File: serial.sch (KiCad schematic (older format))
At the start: 9 parts, among them CN13 RS232, IC1 MAX3232CPWR, J1 TTL, T6 TEST_RS232

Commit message: finished schematic and PCB layout for 1.1 board
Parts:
- removed J1: TTL, telemetry-pcb:molex_sl_1x04_horizontal, symbol Connector:Conn_01x04_Male
- added CN4: UART, telemetry-pcb:Molex-70551-0004-0, symbol Connector_Generic:Conn_01x05
- added J1: Header 02x02, Connector_PinHeader_2.54mm:PinHeader_2x02_P2.54mm_Horizontal, symbol Connector_Generic:Conn_02x02_Odd_Even
- added J2: Header 02x03, Connector_PinHeader_2.54mm:PinHeader_2x03_P2.54mm_Horizontal, symbol Connector_Generic:Conn_02x03_Odd_Even
- added Q1: IF-D92, telemetry-pcb:IF-D92, symbol Device:Q_Photo_NPN
- added R7: 10K, Resistor_SMD:R_0805_2012Metric, symbol Device:R
- renumbered CN13 to CN3, T6 to T5
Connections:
- wire segments 41 -> 64
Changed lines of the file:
@@
 $Descr A4 11693 8268
 encoding utf-8
-Sheet 3 4
+Sheet 2 3
 Title ""
 Date ""
@@
 P 6150 4600
 AR Path="/6199B42E" Ref="#PWR?"  Part="1"
-AR Path="/61951597/6199B42E" Ref="#PWR0119"  Part="1"
-F 0 "#PWR0119" H 6150 4350 50  0001 C CNN
+AR Path="/61951597/6199B42E" Ref="#PWR013"  Part="1"
+F 0 "#PWR013" H 6150 4350 50  0001 C CNN
 F 1 "GND" H 6155 4427 50  0000 C CNN
 F 2 "" H 6150 4600 50  0001 C CNN
@@
 P 6350 2500
 AR Path="/6199B436" Ref="#PWR?"  Part="1"
-AR Path="/61951597/6199B436" Ref="#PWR0120"  Part="1"
-F 0 "#PWR0120" H 6350 2350 50  0001 C CNN
+AR Path="/61951597/6199B436" Ref="#PWR014"  Part="1"
+F 0 "#PWR014" H 6350 2350 50  0001 C CNN
 F 1 "+3V3" H 6365 2673 50  0000 C CNN
 F 2 "" H 6350 2500 50  0001 C CNN
@@
 Wire Wire Line
 	4600 3400 4350 3400
-Text HLabel 9600 3600 2    100  Output ~ 0
+Text HLabel 10450 3000 2    100  Output ~ 0
 RX
-$Comp
-L Connector:Conn_01x04_Male J1
-U 1 1 61C3A8C7
-P 8300 2700
-F 0 "J1" H 8408 2981 50  0000 C CNN
-F 1 "TTL" H 8408 2890 50  0000 C CNN
-F 2 "telemetry-pcb:molex_sl_1x04_horizontal" H 8300 2700 50  0001 C CNN
-F 3 "~" H 8300 2700 50  0001 C CNN
-	1    8300 2700
-	1    0    0    -1
-$EndComp
-Wire Wire Line
-	9600 1900 8700 1900
-Text HLabel 9600 1900 2    100  Output ~ 0
+Text HLabel 10450 2400 2    100  Output ~ 0
 TX
 Wire Wire Line
-	8700 2600 8500 2600
-Connection ~ 8700 1900
-Wire Wire Line
-	8500 2700 8700 2700
-Wire Wire Line
-	8500 2800 8700 2800
-Wire Wire Line
-	8700 3600 9600 3600
-Wire Wire Line
-	8500 2900 8700 2900
-Wire Wire Line
 	4350 1900 4350 3400
-Connection ~ 8700 3600
-Wire Wire Line
-	8700 1900 8700 2600
-Connection ~ 8700 2600
-Wire Wire Line
-	8700 2600 8700 2700
-Wire Wire Line
-	8700 2800 8700 2900
-Connection ~ 8700 2900
-Wire Wire Line
-	8700 2900 8700 3600
 NoConn ~ 7150 5200
 NoConn ~ 7150 5100
@@
 NoConn ~ 7150 4600
 NoConn ~ 7150 4500
-NoConn ~ 7150 4400
 $Comp
 L Connector:Conn_01x02_Female T?
@@
 P 6850 5450
 AR Path="/6199B41D" Ref="T?"  Part="1"
-AR Path="/61951597/6199B41D" Ref="T6"  Part="1"
-F 0 "T6" V 6696 5262 50  0000 R CNN
+AR Path="/61951597/6199B41D" Ref="T5"  Part="1"
+F 0 "T5" V 6696 5262 50  0000 R CNN
 F 1 "TEST_RS232" V 6787 5262 50  0000 R CNN
 F 2 "TestPoint:TestPoint_2Pads_Pitch2.54mm_Drill0.8mm" H 6850 5450 50  0001 C CNN
@@
 P 7450 4800
 AR Path="/6199B3ED" Ref="CN?"  Part="1"
-AR Path="/61951597/6199B3ED" Ref="CN13"  Part="1"
-F 0 "CN13" H 7630 4846 50  0000 L CNN
+AR Path="/61951597/6199B3ED" Ref="CN3"  Part="1"
+F 0 "CN3" H 7630 4846 50  0000 L CNN
 F 1 "RS232" H 7630 4755 50  0000 L CNN
 F 2 "telemetry-pcb:db-9" H 7450 4800 50  0001 C CNN
@@
 P 7050 3300
 AR Path="/6199B40A" Ref="#SUPPLY?"  Part="1"
-AR Path="/61951597/6199B40A" Ref="#SUPPLY0101"  Part="1"
-F 0 "#SUPPLY0101" H 7050 3300 50  0001 C CNN
+AR Path="/61951597/6199B40A" Ref="#SUPPLY01"  Part="1"
+F 0 "#SUPPLY01" H 7050 3300 50  0001 C CNN
 F 1 "GND" H 7050 3200 59  0000 C CNN
 F 2 "" H 7050 3300 50  0001 C CNN
@@
 	6850 5000 7150 5000
 Wire Wire Line
-	4350 1900 8700 1900
-Wire Wire Line
-	6000 3600 8700 3600
+	7150 4400 7000 4400
+Wire Wire Line
+	7000 4400 7000 4100
+Wire Wire Line
+	7000 4100 8250 4100
+$Comp
+L telemetry-pcb-rescue:GND-telemetry-pcb-eagle-import-telemetry-pcb-rescue #SUPPLY?
+U 1 1 62526122
+P 8250 4700
+AR Path="/62526122" Ref="#SUPPLY?"  Part="1"
+AR Path="/61951597/62526122" Ref="#SUPPLY02"  Part="1"
+F 0 "#SUPPLY02" H 8250 4700 50  0001 C CNN
+F 1 "GND" H 8250 4600 59  0000 C CNN
+F 2 "" H 8250 4700 50  0001 C CNN
+F 3 "" H 8250 4700 50  0001 C CNN
+	1    8250 4700
+	1    0    0    -1
+$EndComp
+Wire Wire Line
+	4350 1900 8950 1900
+$Comp
+L Device:Q_Photo_NPN Q1
+U 1 1 625465A1
+P 9250 3650
+F 0 "Q1" H 9440 3696 50  0000 L CNN
+F 1 "IF-D92" H 9440 3605 50  0000 L CNN
+F 2 "telemetry-pcb:IF-D92" H 9450 3750 50  0001 C CNN
+F 3 "~" H 9250 3650 50  0001 C CNN
+	1    9250 3650
+	1    0    0    -1
+$EndComp
+$Comp
+L Device:R R7
+U 1 1 625499FE
+P 9350 4150
+F 0 "R7" H 9420 4196 50  0000 L CNN
+F 1 "10K" H 9420 4105 50  0000 L CNN
+F 2 "Resistor_SMD:R_0805_2012Metric" V 9280 4150 50  0001 C CNN
+F 3 "~" H 9350 4150 50  0001 C CNN
+	1    9350 4150
+	1    0    0    -1
+$EndComp
+Wire Wire Line
+	10050 2350 10250 2350
+Wire Wire Line
+	10250 2350 10250 2400
+Wire Wire Line
+	10250 2400 10450 2400
+Wire Wire Line
+	10050 2450 10250 2450
+Wire Wire Line
+	10250 2450 10250 2400
+Connection ~ 10250 2400
+$Comp
+L Connector_Generic:Conn_02x02_Odd_Even J1
+U 1 1 6254B4AA
+P 9750 2350
+F 0 "J1" H 9800 2567 50  0000 C CNN
+F 1 "Header 02x02" H 9800 2476 50  0000 C CNN
+F 2 "Connector_PinHeader_2.54mm:PinHeader_2x02_P2.54mm_Horizontal" H 9750 2350 50  0001 C CNN
+F 3 "~" H 9750 2350 50  0001 C CNN
+	1    9750 2350
+	1    0    0    -1
+$EndComp
+Wire Wire Line
+	8950 1900 8950 2350
+$Comp
+L Connector_Generic:Conn_01x05 CN4
+U 1 1 62553AD4
+P 7800 2550
+F 0 "CN4" H 7718 2125 50  0000 C CNN
+F 1 "UART" H 7718 2216 50  0000 C CNN
+F 2 "telemetry-pcb:Molex-70551-0004-0" H 7800 2550 50  0001 C CNN
+F 3 "~" H 7800 2550 50  0001 C CNN
+	1    7800 2550
+	-1   0    0    1
+$EndComp
+Wire Wire Line
+	8000 2450 9550 2450
+$Comp
+L power:+3V3 #PWR?
+U 1 1 6255A3E2
+P 8250 2250
+AR Path="/6255A3E2" Ref="#PWR?"  Part="1"
+AR Path="/61951597/6255A3E2" Ref="#PWR015"  Part="1"
+F 0 "#PWR015" H 8250 2100 50  0001 C CNN
+F 1 "+3V3" H 8265 2423 50  0000 C CNN
+F 2 "" H 8250 2250 50  0001 C CNN
+F 3 "" H 8250 2250 50  0001 C CNN
+	1    8250 2250
+	1    0    0    -1
+$EndComp
+Wire Wire Line
+	8000 2350 8250 2350
+Wire Wire Line
+	8250 2350 8250 2250
+$Comp
+L Connector_Generic:Conn_02x03_Odd_Even J2
+U 1 1 6255DD8F
+P 9750 3000
+F 0 "J2" H 9800 3317 50  0000 C CNN
+F 1 "Header 02x03" H 9800 3226 50  0000 C CNN
+F 2 "Connector_PinHeader_2.54mm:PinHeader_2x03_P2.54mm_Horizontal" H 9750 3000 50  0001 C CNN
+F 3 "~" H 9750 3000 50  0001 C CNN
+	1    9750 3000
+	1    0    0    -1
+$EndComp
+Wire Wire Line
+	6000 3600 8950 3600
+Wire Wire Line
+	10050 2900 10250 2900
+Wire Wire Line
+	10250 2900 10250 3000
+Wire Wire Line
+	10250 3000 10450 3000
+Wire Wire Line
+	10050 3000 10250 3000
+Connection ~ 10250 3000
+Wire Wire Line
+	10050 3100 10250 3100
+Wire Wire Line
+	10250 3100 10250 3000
+Wire Wire Line
+	8000 2650 8700 2650
+Wire Wire Line
+	8950 2900 9550 2900
+Wire Wire Line
+	8950 2350 9550 2350
+Wire Wire Line
+	8950 2900 8950 3600
+Wire Wire Line
+	8700 3000 9550 3000
+Wire Wire Line
+	8700 2650 8700 3000
+Wire Wire Line
+	9350 3100 9550 3100
+Wire Wire Line
+	9350 3100 9350 3450
+Wire Wire Line
+	9350 3850 9350 4000
+Wire Wire Line
+	8250 4100 8250 4450
+Wire Wire Line
+	9350 4300 9350 4450
+Wire Wire Line
+	9350 4450 8250 4450
+Connection ~ 8250 4450
+Wire Wire Line
+	8250 4450 8250 4600
+Wire Wire Line
+	8000 2750 8000 3200
+Wire Wire Line
+	8000 3200 7050 3200
+NoConn ~ 8000 2550
 $EndSCHEMATC

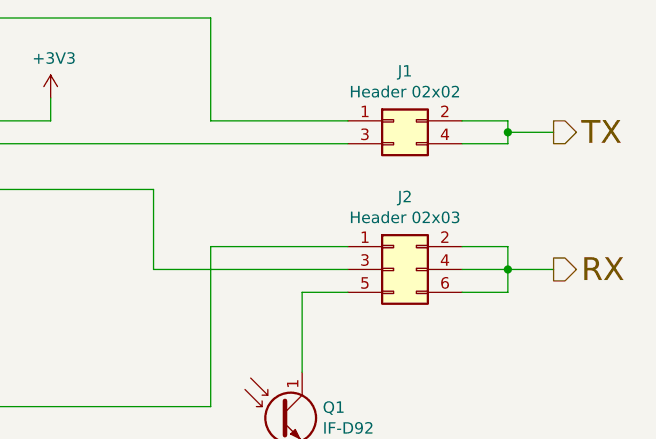
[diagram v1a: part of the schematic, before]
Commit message: removes one power port, changes CAN switch to jumper
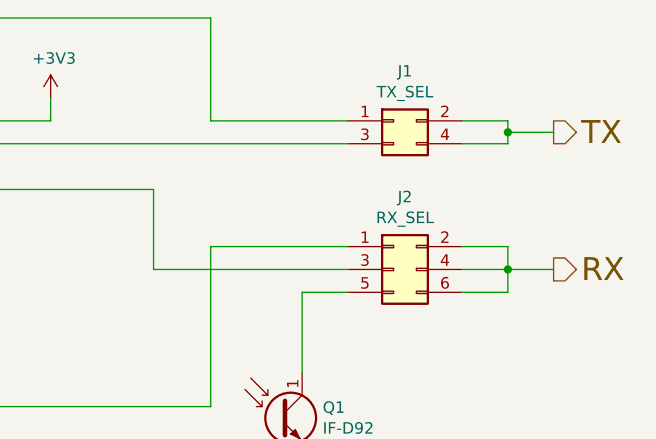
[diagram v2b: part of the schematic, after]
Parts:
- J1: value Header 02x02 -> TX_SEL
- J2: value Header 02x03 -> RX_SEL
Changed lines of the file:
@@
 P 9750 2350
 F 0 "J1" H 9800 2567 50  0000 C CNN
-F 1 "Header 02x02" H 9800 2476 50  0000 C CNN
+F 1 "TX_SEL" H 9800 2476 50  0000 C CNN
 F 2 "Connector_PinHeader_2.54mm:PinHeader_2x02_P2.54mm_Horizontal" H 9750 2350 50  0001 C CNN
 F 3 "~" H 9750 2350 50  0001 C CNN
@@
 P 9750 3000
 F 0 "J2" H 9800 3317 50  0000 C CNN
-F 1 "Header 02x03" H 9800 3226 50  0000 C CNN
+F 1 "RX_SEL" H 9800 3226 50  0000 C CNN
 F 2 "Connector_PinHeader_2.54mm:PinHeader_2x03_P2.54mm_Horizontal" H 9750 3000 50  0001 C CNN
 F 3 "~" H 9750 3000 50  0001 C CNN

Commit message: deleted extraneous footprints
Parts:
- IC1: symbol telemetry-pcb-rescue:MAX3232CPWR-MAX3232CPWR-telemetry-pcb-rescue -> telemetry-pcb-rescue:MAX3232CPWR-MAX3232CPWR-telemetry-pcb-rescue-telemetry-pcb-rescue
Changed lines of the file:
@@
 $EndComp
 $Comp
-L telemetry-pcb-rescue:MAX3232CPWR-MAX3232CPWR-telemetry-pcb-rescue IC?
+L telemetry-pcb-rescue:MAX3232CPWR-MAX3232CPWR-telemetry-pcb-rescue-telemetry-pcb-rescue IC?
 U 1 1 6199B43C
 P 5300 3800
@@
 	7050 2800 7050 3200
 $Comp
-L telemetry-pcb-rescue:GND-telemetry-pcb-eagle-import-telemetry-pcb-rescue #SUPPLY?
+L telemetry-pcb-rescue:GND-telemetry-pcb-eagle-import-telemetry-pcb-rescue-telemetry-pcb-rescue #SUPPLY?
 U 1 1 6199B40A
 P 7050 3300
@@
 	7000 4100 8250 4100
 $Comp
-L telemetry-pcb-rescue:GND-telemetry-pcb-eagle-import-telemetry-pcb-rescue #SUPPLY?
+L telemetry-pcb-rescue:GND-telemetry-pcb-eagle-import-telemetry-pcb-rescue-telemetry-pcb-rescue #SUPPLY?
 U 1 1 62526122
 P 8250 4700

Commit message: minor changes to serial port - update rs232 connector and delete GND connection
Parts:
- CN3: footprint telemetry-pcb:db-9 -> Connector_Dsub:DSUB-9_Female_Horizontal_P2.77x2.84mm_EdgePinOffset7.70mm_Housed_MountingHolesOffset9.12mm; symbol Connector:DB9_Male -> Connector:DB9_Female
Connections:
- net at IC1.14 (DOUT1), T5.1 (Pin_1): now also CN3.3; no longer CN3.2
- net at IC1.13 (RIN1), T5.2 (Pin_2): now also CN3.2; no longer CN3.3
- net at CN3.5: no longer R7.2
- no-connect marks 11 -> 12
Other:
- moved on the sheet: T5
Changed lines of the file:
@@
 $EndComp
-Wire Wire Line
-	4050 3600 4050 4800
 Wire Wire Line
 	4600 3400 4350 3400
@@
 Wire Wire Line
 	4350 1900 4350 3400
-NoConn ~ 7150 5200
 NoConn ~ 7150 5100
 NoConn ~ 7150 4900
 NoConn ~ 7150 4700
-NoConn ~ 7150 4600
 NoConn ~ 7150 4500
 $Comp
 L Connector:Conn_01x02_Female T?
 U 1 1 6199B41D
-P 6850 5450
+P 6750 5350
 AR Path="/6199B41D" Ref="T?"  Part="1"
 AR Path="/61951597/6199B41D" Ref="T5"  Part="1"
-F 0 "T5" V 6696 5262 50  0000 R CNN
-F 1 "TEST_RS232" V 6787 5262 50  0000 R CNN
-F 2 "TestPoint:TestPoint_2Pads_Pitch2.54mm_Drill0.8mm" H 6850 5450 50  0001 C CNN
-F 3 "~" H 6850 5450 50  0001 C CNN
-	1    6850 5450
+F 0 "T5" V 6596 5162 50  0000 R CNN
+F 1 "TEST_RS232" V 6687 5162 50  0000 R CNN
+F 2 "TestPoint:TestPoint_2Pads_Pitch2.54mm_Drill0.8mm" H 6750 5350 50  0001 C CNN
+F 3 "~" H 6750 5350 50  0001 C CNN
+	1    6750 5350
 	0    1    1    0
 $EndComp
 $Comp
-L Connector:DB9_Male CN?
+L Connector:DB9_Female CN?
 U 1 1 6199B3ED
 P 7450 4800
@@
 F 0 "CN3" H 7630 4846 50  0000 L CNN
 F 1 "RS232" H 7630 4755 50  0000 L CNN
-F 2 "telemetry-pcb:db-9" H 7450 4800 50  0001 C CNN
+F 2 "Connector_Dsub:DSUB-9_Female_Horizontal_P2.77x2.84mm_EdgePinOffset7.70mm_Housed_MountingHolesOffset9.12mm" H 7450 4800 50  0001 C CNN
 F 3 " ~" H 7450 4800 50  0001 C CNN
 	1    7450 4800
@@
 	6350 2800 6350 3100
 Wire Wire Line
-	6850 5250 6850 5000
-Connection ~ 6850 5000
-Wire Wire Line
-	4050 4800 6750 4800
-Wire Wire Line
-	6850 3400 6850 5000
+	4050 5000 6650 5000
 Wire Wire Line
 	6000 3400 6850 3400
-Wire Wire Line
-	6750 4800 6750 5250
-Connection ~ 6750 4800
-Wire Wire Line
-	6750 4800 7150 4800
-Wire Wire Line
-	6850 5000 7150 5000
-Wire Wire Line
-	7150 4400 7000 4400
-Wire Wire Line
-	7000 4400 7000 4100
-Wire Wire Line
-	7000 4100 8250 4100
 $Comp
 L telemetry-pcb-rescue:GND-telemetry-pcb-eagle-import-telemetry-pcb-rescue-telemetry-pcb-rescue #SUPPLY?
 U 1 1 62526122
-P 8250 4700
+P 9350 4550
 AR Path="/62526122" Ref="#SUPPLY?"  Part="1"
 AR Path="/61951597/62526122" Ref="#SUPPLY02"  Part="1"
-F 0 "#SUPPLY02" H 8250 4700 50  0001 C CNN
-F 1 "GND" H 8250 4600 59  0000 C CNN
-F 2 "" H 8250 4700 50  0001 C CNN
-F 3 "" H 8250 4700 50  0001 C CNN
-	1    8250 4700
+F 0 "#SUPPLY02" H 9350 4550 50  0001 C CNN
+F 1 "GND" H 9350 4450 59  0000 C CNN
+F 2 "" H 9350 4550 50  0001 C CNN
+F 3 "" H 9350 4550 50  0001 C CNN
+	1    9350 4550
 	1    0    0    -1
 $EndComp
@@
 	9350 3850 9350 4000
 Wire Wire Line
-	8250 4100 8250 4450
-Wire Wire Line
 	9350 4300 9350 4450
-Wire Wire Line
-	9350 4450 8250 4450
-Connection ~ 8250 4450
-Wire Wire Line
-	8250 4450 8250 4600
 Wire Wire Line
 	8000 2750 8000 3200
@@
 	8000 3200 7050 3200
 NoConn ~ 8000 2550
+NoConn ~ 7150 4400
+Wire Wire Line
+	6850 3400 6850 4800
+Wire Wire Line
+	6850 4800 7150 4800
+Wire Wire Line
+	4050 3600 4050 5000
+Wire Wire Line
+	6650 4600 6650 5000
+Wire Wire Line
+	6650 4600 7150 4600
+NoConn ~ 7150 5000
+Wire Wire Line
+	6650 5000 6650 5150
+Connection ~ 6650 5000
+Wire Wire Line
+	6850 4800 6850 5150
+Wire Wire Line
+	6850 5150 6750 5150
+Connection ~ 6850 4800
+NoConn ~ 7150 5200
 $EndSCHEMATC

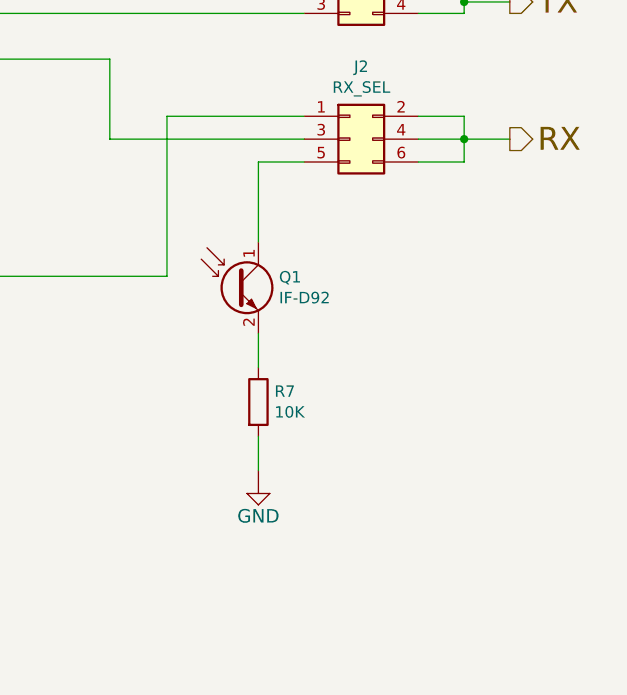
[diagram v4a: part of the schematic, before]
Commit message: fixes optical receiver wiring and changes GPS connector to JST GH
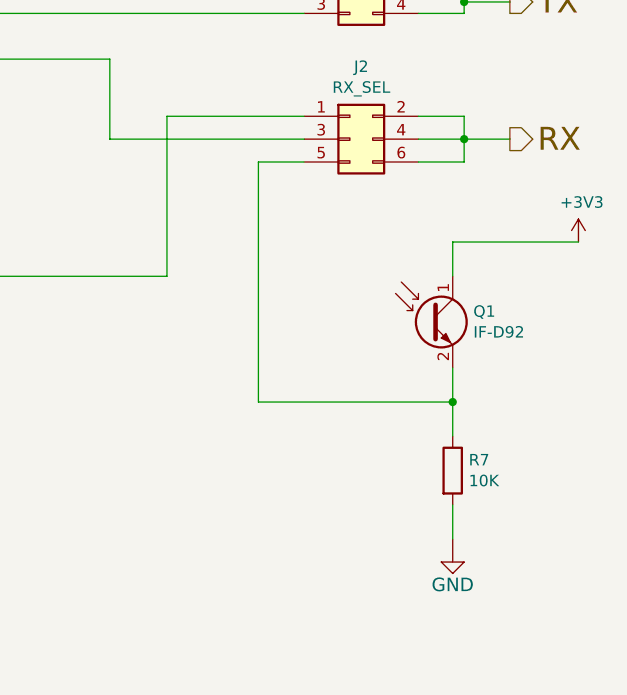
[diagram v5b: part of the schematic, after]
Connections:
- net +3V3: now also Q1.1 (C)
- net at J2.5 (Pin_5): now also Q1.2 (E), R7.1; no longer Q1.1 (C)
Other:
- moved on the sheet: Q1, R7
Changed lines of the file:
@@
 L telemetry-pcb-rescue:GND-telemetry-pcb-eagle-import-telemetry-pcb-rescue-telemetry-pcb-rescue #SUPPLY?
 U 1 1 62526122
-P 9350 4550
+P 10200 4850
 AR Path="/62526122" Ref="#SUPPLY?"  Part="1"
 AR Path="/61951597/62526122" Ref="#SUPPLY02"  Part="1"
-F 0 "#SUPPLY02" H 9350 4550 50  0001 C CNN
-F 1 "GND" H 9350 4450 59  0000 C CNN
-F 2 "" H 9350 4550 50  0001 C CNN
-F 3 "" H 9350 4550 50  0001 C CNN
-	1    9350 4550
+F 0 "#SUPPLY02" H 10200 4850 50  0001 C CNN
+F 1 "GND" H 10200 4750 59  0000 C CNN
+F 2 "" H 10200 4850 50  0001 C CNN
+F 3 "" H 10200 4850 50  0001 C CNN
+	1    10200 4850
 	1    0    0    -1
 $EndComp
@@
 L Device:Q_Photo_NPN Q1
 U 1 1 625465A1
-P 9250 3650
-F 0 "Q1" H 9440 3696 50  0000 L CNN
-F 1 "IF-D92" H 9440 3605 50  0000 L CNN
-F 2 "telemetry-pcb:IF-D92" H 9450 3750 50  0001 C CNN
-F 3 "~" H 9250 3650 50  0001 C CNN
-	1    9250 3650
+P 10100 3800
+F 0 "Q1" H 10290 3846 50  0000 L CNN
+F 1 "IF-D92" H 10290 3755 50  0000 L CNN
+F 2 "telemetry-pcb:IF-D92" H 10300 3900 50  0001 C CNN
+F 3 "~" H 10100 3800 50  0001 C CNN
+	1    10100 3800
 	1    0    0    -1
 $EndComp
@@
 L Device:R R7
 U 1 1 625499FE
-P 9350 4150
-F 0 "R7" H 9420 4196 50  0000 L CNN
-F 1 "10K" H 9420 4105 50  0000 L CNN
-F 2 "Resistor_SMD:R_0805_2012Metric" V 9280 4150 50  0001 C CNN
-F 3 "~" H 9350 4150 50  0001 C CNN
-	1    9350 4150
+P 10200 4450
+F 0 "R7" H 10270 4496 50  0000 L CNN
+F 1 "10K" H 10270 4405 50  0000 L CNN
+F 2 "Resistor_SMD:R_0805_2012Metric" V 10130 4450 50  0001 C CNN
+F 3 "~" H 10200 4450 50  0001 C CNN
+	1    10200 4450
 	1    0    0    -1
 $EndComp
@@
 	9350 3100 9550 3100
 Wire Wire Line
-	9350 3100 9350 3450
+	10200 4150 10200 4300
 Wire Wire Line
-	9350 3850 9350 4000
-Wire Wire Line
-	9350 4300 9350 4450
+	10200 4600 10200 4750
 Wire Wire Line
 	8000 2750 8000 3200
@@
 Connection ~ 6850 4800
 NoConn ~ 7150 5200
+Wire Wire Line
+	9350 4150 10200 4150
+Wire Wire Line
+	9350 3100 9350 4150
+Wire Wire Line
+	10200 4000 10200 4150
+Connection ~ 10200 4150
+$Comp
+L power:+3V3 #PWR?
+U 1 1 62EA7564
+P 10750 3450
+AR Path="/62EA7564" Ref="#PWR?"  Part="1"
+AR Path="/61951597/62EA7564" Ref="#PWR0102"  Part="1"
+F 0 "#PWR0102" H 10750 3300 50  0001 C CNN
+F 1 "+3V3" H 10765 3623 50  0000 C CNN
+F 2 "" H 10750 3450 50  0001 C CNN
+F 3 "" H 10750 3450 50  0001 C CNN
+	1    10750 3450
+	1    0    0    -1
+$EndComp
+Wire Wire Line
+	10750 3450 10200 3450
+Wire Wire Line
+	10200 3450 10200 3600
 $EndSCHEMATC

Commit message: some more small changes from design review
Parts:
- CN4: footprint telemetry-pcb:Molex-70551-0004-0 -> telemetry-pcb:molex_sl_1x04_horizontal; symbol Connector_Generic:Conn_01x05 -> Connector_Generic:Conn_01x04
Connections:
- net +3V3: now also CN4.4 (Pin_4), R7.1; no longer CN4.5 (Pin_5), Q1.1 (C)
- net at R7.2: now also J2.5 (Pin_5), Q1.1 (C)
- net at J1.3 (Pin_3): now also CN4.3 (Pin_3); no longer CN4.4 (Pin_4)
- now unconnected: Q1.2 (E)
- no-connect marks 12 -> 11
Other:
- moved on the sheet: Q1, R7
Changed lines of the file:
@@
 L Device:Q_Photo_NPN Q1
 U 1 1 625465A1
-P 10100 3800
-F 0 "Q1" H 10290 3846 50  0000 L CNN
-F 1 "IF-D92" H 10290 3755 50  0000 L CNN
-F 2 "telemetry-pcb:IF-D92" H 10300 3900 50  0001 C CNN
-F 3 "~" H 10100 3800 50  0001 C CNN
-	1    10100 3800
+P 10100 4300
+F 0 "Q1" H 10290 4346 50  0000 L CNN
+F 1 "IF-D92" H 10290 4255 50  0000 L CNN
+F 2 "telemetry-pcb:IF-D92" H 10300 4400 50  0001 C CNN
+F 3 "~" H 10100 4300 50  0001 C CNN
+	1    10100 4300
 	1    0    0    -1
 $EndComp
@@
 L Device:R R7
 U 1 1 625499FE
-P 10200 4450
-F 0 "R7" H 10270 4496 50  0000 L CNN
-F 1 "10K" H 10270 4405 50  0000 L CNN
-F 2 "Resistor_SMD:R_0805_2012Metric" V 10130 4450 50  0001 C CNN
-F 3 "~" H 10200 4450 50  0001 C CNN
-	1    10200 4450
+P 10200 3750
+F 0 "R7" H 10270 3796 50  0000 L CNN
+F 1 "10K" H 10270 3705 50  0000 L CNN
+F 2 "Resistor_SMD:R_0805_2012Metric" V 10130 3750 50  0001 C CNN
+F 3 "~" H 10200 3750 50  0001 C CNN
+	1    10200 3750
 	1    0    0    -1
 $EndComp
@@
 	8950 1900 8950 2350
 $Comp
-L Connector_Generic:Conn_01x05 CN4
+L Connector_Generic:Conn_01x04 CN4
 U 1 1 62553AD4
 P 7800 2550
 F 0 "CN4" H 7718 2125 50  0000 C CNN
 F 1 "UART" H 7718 2216 50  0000 C CNN
-F 2 "telemetry-pcb:Molex-70551-0004-0" H 7800 2550 50  0001 C CNN
+F 2 "telemetry-pcb:molex_sl_1x04_horizontal" H 7800 2550 50  0001 C CNN
 F 3 "~" H 7800 2550 50  0001 C CNN
 	1    7800 2550
@@
 	10250 3100 10250 3000
 Wire Wire Line
-	8000 2650 8700 2650
-Wire Wire Line
 	8950 2900 9550 2900
 Wire Wire Line
@@
 	8700 3000 9550 3000
 Wire Wire Line
-	8700 2650 8700 3000
-Wire Wire Line
 	9350 3100 9550 3100
 Wire Wire Line
-	10200 4150 10200 4300
-Wire Wire Line
-	10200 4600 10200 4750
-Wire Wire Line
-	8000 2750 8000 3200
-Wire Wire Line
 	8000 3200 7050 3200
-NoConn ~ 8000 2550
 NoConn ~ 7150 4400
 Wire Wire Line
@@
 Connection ~ 6850 4800
 NoConn ~ 7150 5200
-Wire Wire Line
-	9350 4150 10200 4150
-Wire Wire Line
-	9350 3100 9350 4150
-Wire Wire Line
-	10200 4000 10200 4150
-Connection ~ 10200 4150
 $Comp
 L power:+3V3 #PWR?
@@
 Wire Wire Line
 	10200 3450 10200 3600
+Wire Wire Line
+	8700 2550 8000 2550
+Wire Wire Line
+	8700 2550 8700 3000
+Wire Wire Line
+	8000 2650 8000 3200
+Wire Wire Line
+	9350 3100 9350 4000
+Wire Wire Line
+	9350 4000 10200 4000
+Wire Wire Line
+	10200 4000 10200 3900
+Wire Wire Line
+	10200 4000 10200 4100
+Connection ~ 10200 4000
+Wire Wire Line
+	10200 4500 10200 4750
 $EndSCHEMATC
